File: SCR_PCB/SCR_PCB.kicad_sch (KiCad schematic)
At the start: 4 parts, among them J1 RJ45, J2 Conn_01x03, U2 NA555D, U3 MAX941xSA

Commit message: update SRC_PCB
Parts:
- removed U3: MAX941xSA, Package_SO:SOIC-8_3.9x4.9mm_P1.27mm, symbol Comparator:MAX941xSA
- added C1, C12, C13, C14, C15, C16, C2, C7: 1u, symbol Device:C
- added D1: D, symbol Device:D
- added D2: SP0502BAHT, Package_TO_SOT_SMD:SOT-23, symbol Power_Protection:SP0502BAHT
- added JP1: Jumper_2_Bridged, symbol Jumper:Jumper_2_Bridged
- added R1, R2, R28, R3, R4, R5: R, symbol Device:R
- added R11, R27: 1k, symbol Device:R
- added R29, R30: 100r, symbol Device:R
- added RV1: R_Potentiometer, symbol Device:R_Potentiometer
- added U3: NA555D, Package_SO:SOIC-8_3.9x4.9mm_P1.27mm, symbol Timer:NA555D
- added U5, U6: SFH617A-1, Package_DIP:DIP-4_W7.62mm, symbol Isolator:SFH617A-1
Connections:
- net +5V: now also U2.8 (VCC), C14.1, C2.1, D1.1 (K), R11.1, R27.1, R28.1, R5.1, U3.8 (VCC); no longer J2.3 (Pin_3)
- net GND: now also U2.1 (GND), C1.2, C12.2, C13.2, C14.2, C15.2, C16.2, C2.2, C7.2, D2.3 (A), JP1.1 (A), R30.1, RV1.2, U3.1 (GND)
- net enable: now also U2.4 (~{RST}), R29.2, R30.2, U3.4 (~{RST}); no longer J2.2 (Pin_2)
- net at U2.2 (TRIG): now also C15.1, R5.2, U5.4
- net SCR 2/TRG: now reaches U2.3 (OUT)
- net at U2.5 (CONT): now also C7.1
- net at U2.6 (THRES): now also U2.7 (DISCH), C1.1, R11.2
- new net: JP1.2 (B), RV1.1, U5.3, U6.3
- new net: D2.1 (K), J2.2 (Pin_2), R29.1
- new net: D1.2 (A), D2.2 (K), J2.3 (Pin_3)
- new net: R3.2, R4.1
- new net: R4.2, U5.1, U6.2
- new net: R1.2, R2.1
- new net: R2.2, R3.1
- new net: C12.1, U3.5 (CONT)
- new net: C16.1, R28.2, U3.2 (TRIG), U6.4
- new net: C13.1, R27.2, U3.6 (THRES), U3.7 (DISCH)
- new net: U5.2, U6.1
- new net SCR 1/TRG: U3.3 (OUT)
- no-connect marks 0 -> 1
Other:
- added sheet SCR 2 (untitled.kicad_sch)
- added sheet SCR 3 (untitled.kicad_sch)
- added sheet SCR 4 (untitled.kicad_sch)
- sheet SCR 1 ports: added GATE, Kathode, TRG; removed none
- note added: "Neutral"
- note added: "live"
- moved on the sheet: J1, J2, U2

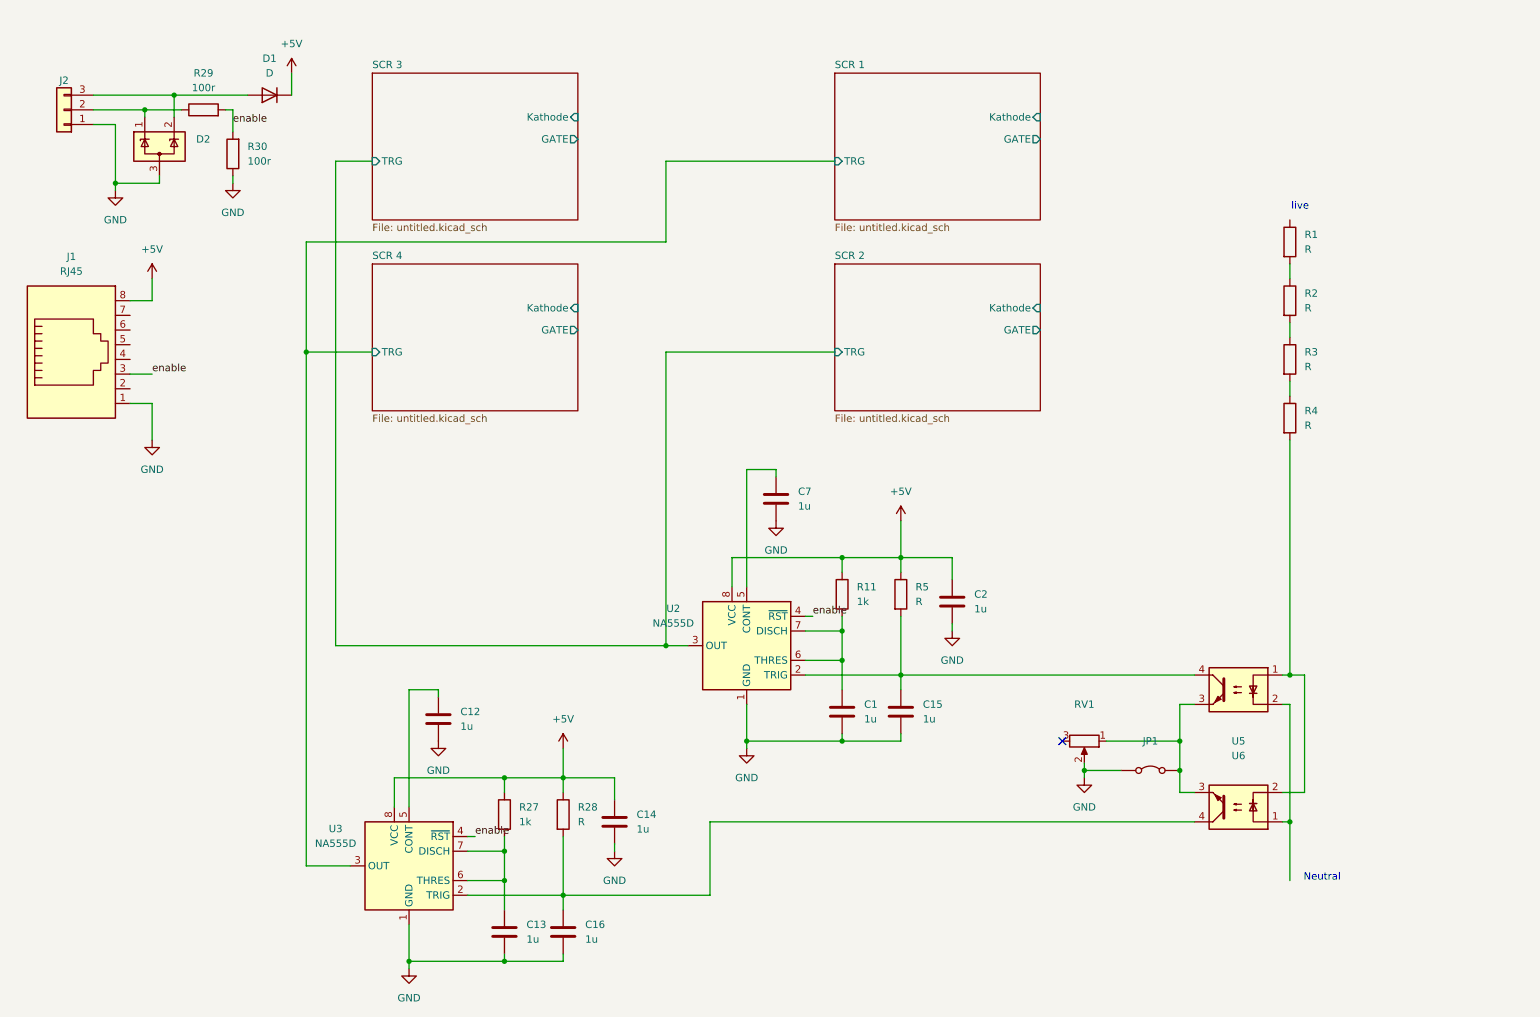
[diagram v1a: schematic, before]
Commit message: add SCR PCB
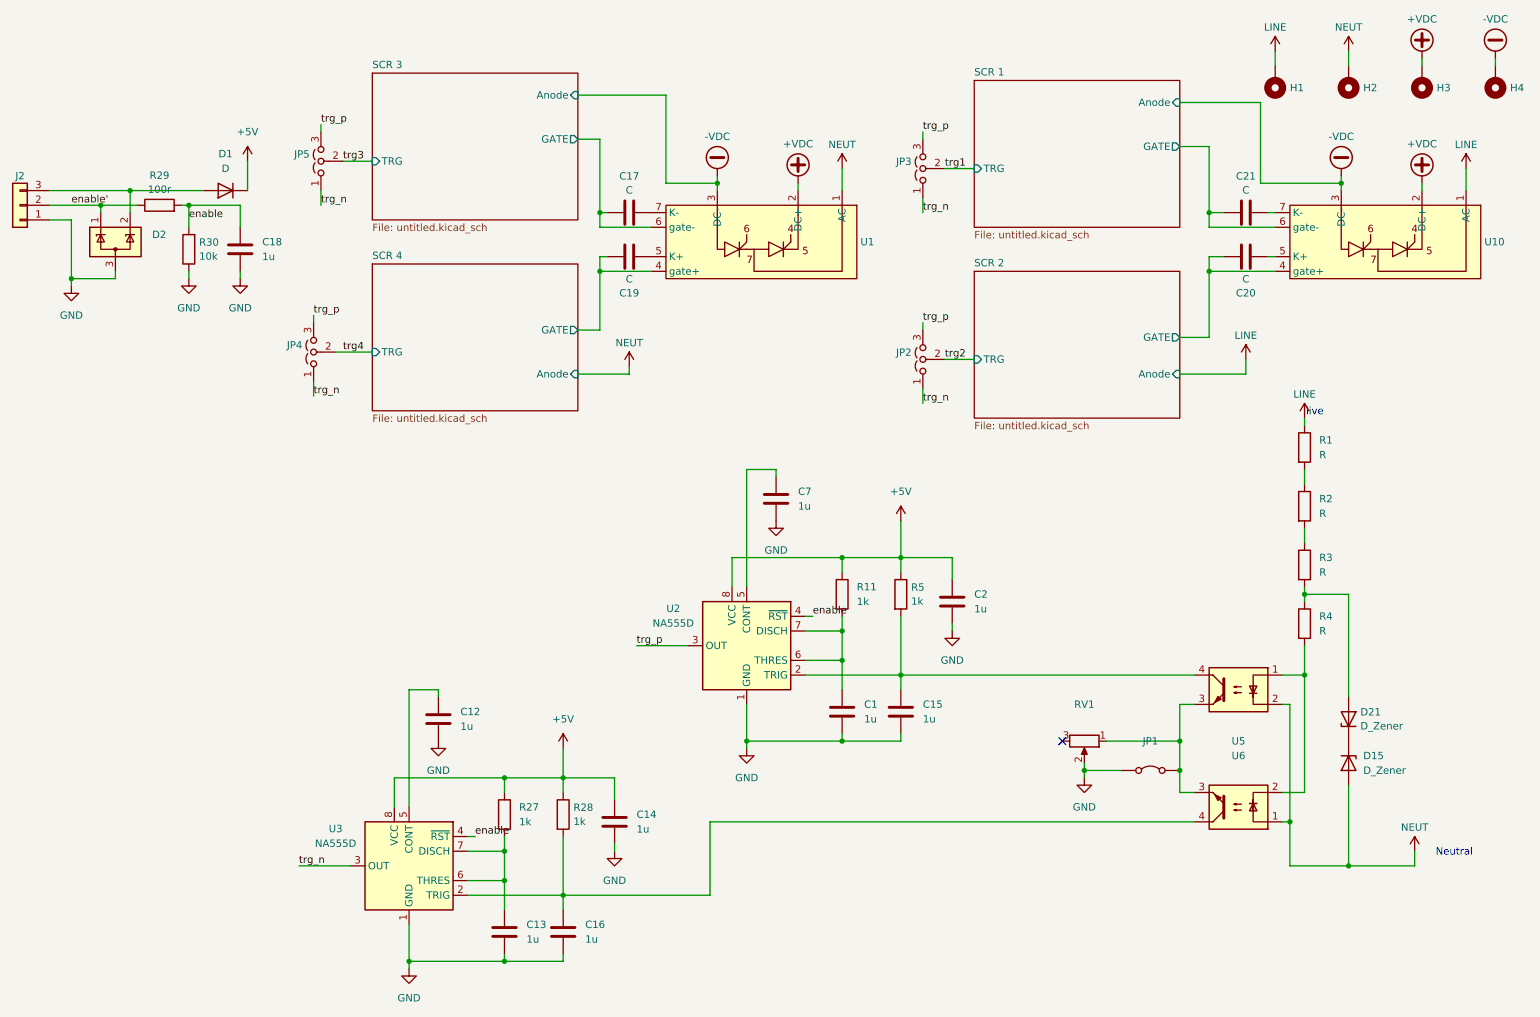
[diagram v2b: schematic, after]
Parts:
- removed J1: RJ45, symbol Connector:RJ45
- added C17, C19, C20, C21: C, Capacitor_THT:C_Axial_L5.1mm_D3.1mm_P15.00mm_Horizontal, symbol Device:C
- added C18: 1u, Capacitor_SMD:C_0805_2012Metric, symbol Device:C
- added D15, D21: D_Zener, Diode_SMD:D_SMA, symbol Device:D_Zener
- added H1, H2, H3, H4: MountingHole_Pad, MountingHole:MountingHole_5.3mm_M5_Pad_Via, symbol Mechanical:MountingHole_Pad
- added JP2, JP3, JP4, JP5: Jumper_3_Open, Jumper:SolderJumper-3_P1.3mm_Bridged2Bar123_RoundedPad1.0x1.5mm_NumberLabels, symbol Jumper:Jumper_3_Open
- added U1, U10: (no value), Library:scr, symbol New_Library:SCR
- C1, C12, C13, C14, C15, C16, C2, C7: footprint (none) -> Capacitor_SMD:C_0805_2012Metric
- D1: footprint (none) -> Diode_SMD:D_SMA
- J2: footprint (none) -> Connector_Molex:Molex_SL_171971-0003_1x03_P2.54mm_Vertical
- JP1: footprint (none) -> Jumper:SolderJumper-2_P1.3mm_Bridged2Bar_RoundedPad1.0x1.5mm
- R1, R2, R3, R4: footprint (none) -> Resistor_SMD:R_1206_3216Metric
- R11, R27, R29: footprint (none) -> Resistor_SMD:R_0805_2012Metric
- R28, R5: value R -> 1k; footprint (none) -> Resistor_SMD:R_0805_2012Metric
- R30: value 100r -> 10k; footprint (none) -> Resistor_SMD:R_0805_2012Metric
- RV1: footprint (none) -> Potentiometer_SMD:Potentiometer_ACP_CA6-VSMD_Vertical
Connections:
- net GND: now also C18.2
- net SCR 1/GATE: now also C21.1, U10.6 (gate-)
- net SCR 2/GATE: now also C20.1, U10.4 (gate+)
- net SCR 3/GATE: now also C17.1, U1.6 (gate-)
- net SCR 4/GATE: now also C19.1, U1.4 (gate+)
- net enable: now also C18.1
- net enable': now reaches D2.1 (K), J2.2 (Pin_2), R29.1
- net at R3.2, R4.1: now also D21.2 (A)
- net NEUT: now reaches U5.2, U6.1
- net NEUT: now also D15.2 (A), H2.1, U1.1 (AC)
- net LINE: now reaches R1.1
- net LINE: now also H1.1, U10.1 (AC)
- net SCR 1/TRG renamed trg_n
- net trg_n: now also JP2.1 (A), JP3.1 (A), JP4.1 (A), JP5.1 (A)
- net SCR 2/TRG renamed trg_p
- net trg_p: now also JP2.3 (B), JP3.3 (B), JP4.3 (B), JP5.3 (B)
- new net: C19.2, U1.5 (K+)
- new net: C20.2, U10.5 (K+)
- new net: C21.2, U10.7 (K-)
- new net: C17.2, U1.7 (K-)
- new net: D15.1 (K), D21.1 (K)
- new net +VDC: H3.1, U1.2 (DC+), U10.2 (DC+)
- new net -VDC: H4.1, U1.3 (DC-), U10.3 (DC-)
- new net trg1: JP3.2 (C)
- new net trg2: JP2.2 (C)
- new net trg3: JP5.2 (C)
- new net trg4: JP4.2 (C)
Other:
- sheet SCR 1 ports: added Anode; removed Kathode
- sheet SCR 2 ports: added Anode; removed Kathode
- sheet SCR 3 ports: added Anode; removed Kathode
- sheet SCR 4 ports: added Anode; removed Kathode
- moved on the sheet: D1, D2, J2, R1, R2, R29, R3, R30, R4
